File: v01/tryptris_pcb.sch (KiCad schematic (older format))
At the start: 131 parts, among them J1 USB_C_Receptacle_USB2.0, J2 I2C-L, J3 I2C-R, SW1 Reset, U1 ATmega32U4-AU, U2 MCP23017_SO, Y1 16Mhz

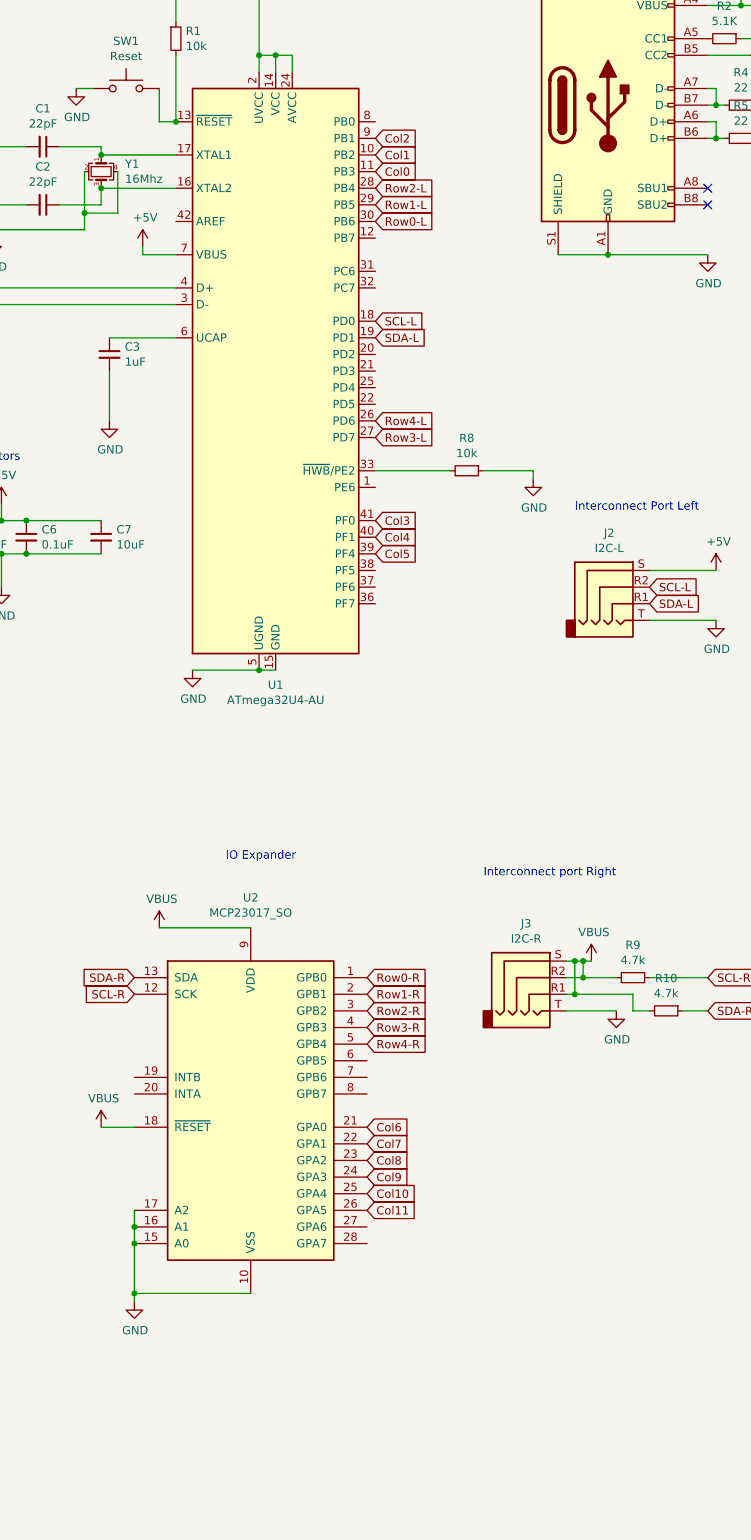
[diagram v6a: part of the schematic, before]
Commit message: Fix ERC and DRC errors.
Move right half to use VSS instead of GND and add power flags to remove
net links between sides.
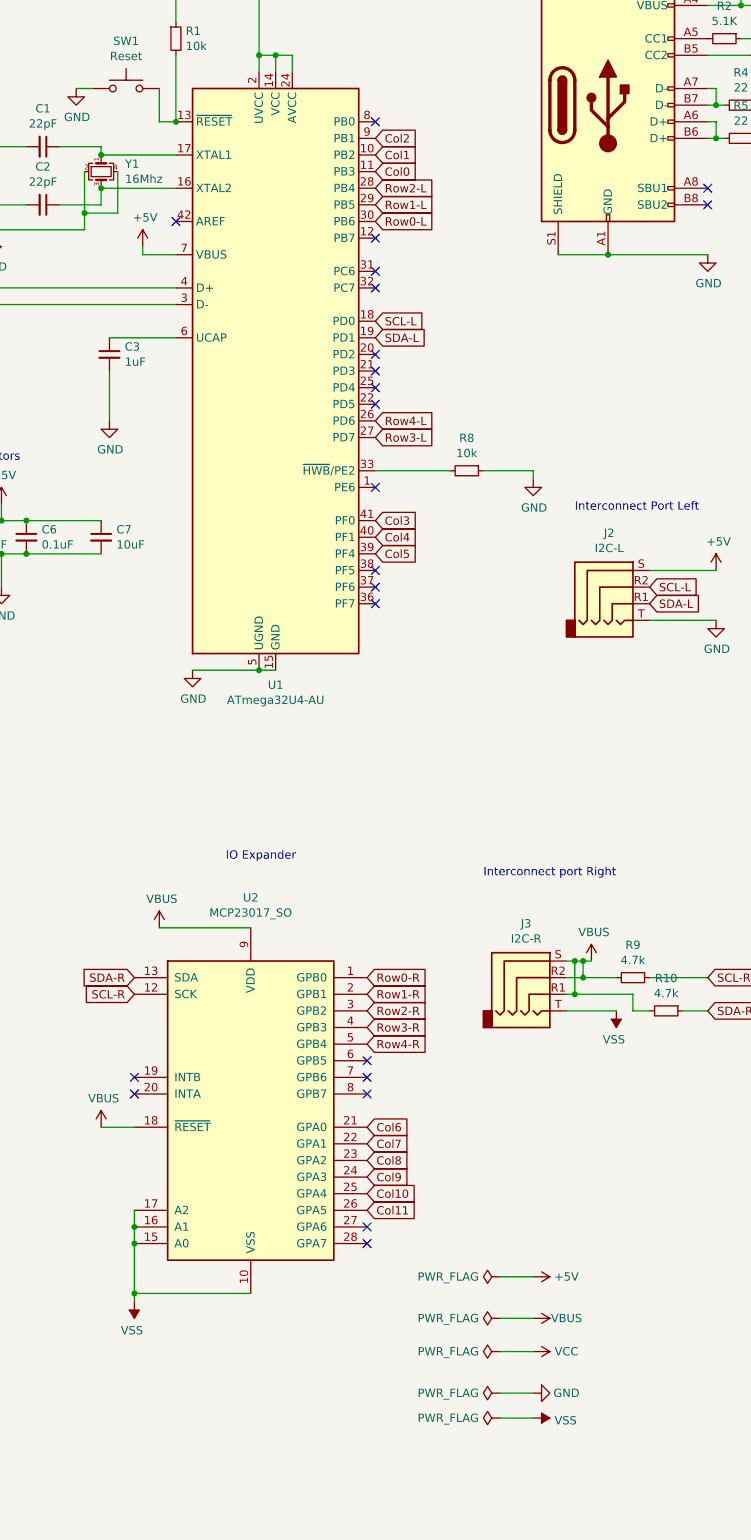
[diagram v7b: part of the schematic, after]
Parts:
- SW1: footprint random-keyboard-parts:PushButton_6x6mm_TH -> random-keyboard-parts:SKQG-1155865
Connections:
- net GND: no longer J3.T, U2.10 (VSS), U2.15 (A0), U2.16 (A1), U2.17 (A2)
- new net VSS: J3.T, U2.10 (VSS), U2.15 (A0), U2.16 (A1), U2.17 (A2)
- no-connect marks 2 -> 22
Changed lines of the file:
@@
 F 0 "SW1" H 2200 1835 50  0000 C CNN
 F 1 "Reset" H 2200 1744 50  0000 C CNN
-F 2 "random-keyboard-parts:PushButton_6x6mm_TH" H 2200 1750 50  0001 C CNN
+F 2 "random-keyboard-parts:SKQG-1155865" H 2200 1750 50  0001 C CNN
 F 3 "~" H 2200 1750 50  0001 C CNN
 	1    2200 1550
@@
 Text GLabel 3650 8300 2    50   Input ~ 0
 Col11
-$Comp
-L power:GND #PWR0114
-U 1 1 613EDEC9
-P 2250 8850
-F 0 "#PWR0114" H 2250 8600 50  0001 C CNN
-F 1 "GND" H 2255 8677 50  0000 C CNN
-F 2 "" H 2250 8850 50  0001 C CNN
-F 3 "" H 2250 8850 50  0001 C CNN
-	1    2250 8850
-	1    0    0    -1
-$EndComp
 Wire Wire Line
 	2950 8800 2250 8800
@@
 Wire Wire Line
 	5750 4750 5350 4750
-$Comp
-L power:GND #PWR0118
-U 1 1 61752755
-P 5150 7100
-F 0 "#PWR0118" H 5150 6850 50  0001 C CNN
-F 1 "GND" H 5155 6927 50  0000 C CNN
-F 2 "" H 5150 7100 50  0001 C CNN
-F 3 "" H 5150 7100 50  0001 C CNN
-	1    5150 7100
-	1    0    0    -1
-$EndComp
 Wire Wire Line
 	5150 7100 4850 7100
@@
 Wire Wire Line
 	1050 2750 2500 2750
+$Comp
+L power:PWR_FLAG #FLG0101
+U 1 1 617813AB
+P 4450 9400
+F 0 "#FLG0101" H 4450 9475 50  0001 C CNN
+F 1 "PWR_FLAG" V 4450 9527 50  0000 L CNN
+F 2 "" H 4450 9400 50  0001 C CNN
+F 3 "~" H 4450 9400 50  0001 C CNN
+	1    4450 9400
+	0    -1   -1   0
+$EndComp
+$Comp
+L power:GND #PWR0111
+U 1 1 61781F62
+P 4650 9400
+F 0 "#PWR0111" H 4650 9150 50  0001 C CNN
+F 1 "GND" V 4650 9200 50  0000 C CNN
+F 2 "" H 4650 9400 50  0001 C CNN
+F 3 "" H 4650 9400 50  0001 C CNN
+	1    4650 9400
+	0    -1   -1   0
+$EndComp
+Wire Wire Line
+	4450 9400 4650 9400
+$Comp
+L power:PWR_FLAG #FLG0102
+U 1 1 6179D4FD
+P 4450 8950
+F 0 "#FLG0102" H 4450 9025 50  0001 C CNN
+F 1 "PWR_FLAG" V 4450 9077 50  0000 L CNN
+F 2 "" H 4450 8950 50  0001 C CNN
+F 3 "~" H 4450 8950 50  0001 C CNN
+	1    4450 8950
+	0    -1   -1   0
+$EndComp
+Wire Wire Line
+	4450 8950 4650 8950
+NoConn ~ 2500 2350
+NoConn ~ 3700 2450
+NoConn ~ 3700 2650
+NoConn ~ 3700 2750
+NoConn ~ 3700 3150
+NoConn ~ 3700 3250
+NoConn ~ 3700 3350
+NoConn ~ 3700 3450
+NoConn ~ 3700 3950
+NoConn ~ 3700 4450
+NoConn ~ 3700 4550
+NoConn ~ 3700 4650
+NoConn ~ 3650 7400
+NoConn ~ 3650 7500
+NoConn ~ 3650 7600
+NoConn ~ 3650 8400
+NoConn ~ 3650 8500
+NoConn ~ 2250 7500
+NoConn ~ 2250 7600
+$Comp
+L power:PWR_FLAG #FLG0103
+U 1 1 61975930
+P 4450 8700
+F 0 "#FLG0103" H 4450 8775 50  0001 C CNN
+F 1 "PWR_FLAG" V 4450 8827 50  0000 L CNN
+F 2 "" H 4450 8700 50  0001 C CNN
+F 3 "~" H 4450 8700 50  0001 C CNN
+	1    4450 8700
+	0    -1   -1   0
+$EndComp
+$Comp
+L power:+5V #PWR0113
+U 1 1 6197725E
+P 4650 8700
+F 0 "#PWR0113" H 4650 8550 50  0001 C CNN
+F 1 "+5V" V 4650 8900 50  0000 C CNN
+F 2 "" H 4650 8700 50  0001 C CNN
+F 3 "" H 4650 8700 50  0001 C CNN
+	1    4650 8700
+	0    1    1    0
+$EndComp
+Wire Wire Line
+	4650 8700 4450 8700
+NoConn ~ 3700 1750
+$Comp
+L power:PWR_FLAG #FLG0104
+U 1 1 619BC24A
+P 4450 9150
+F 0 "#FLG0104" H 4450 9225 50  0001 C CNN
+F 1 "PWR_FLAG" V 4450 9277 50  0000 L CNN
+F 2 "" H 4450 9150 50  0001 C CNN
+F 3 "~" H 4450 9150 50  0001 C CNN
+	1    4450 9150
+	0    -1   -1   0
+$EndComp
+$Comp
+L power:VCC #PWR0115
+U 1 1 619BCAA9
+P 4650 9150
+F 0 "#PWR0115" H 4650 9000 50  0001 C CNN
+F 1 "VCC" V 4650 9350 50  0000 C CNN
+F 2 "" H 4650 9150 50  0001 C CNN
+F 3 "" H 4650 9150 50  0001 C CNN
+	1    4650 9150
+	0    1    1    0
+$EndComp
+Wire Wire Line
+	4650 9150 4450 9150
+$Comp
+L power:VSS #PWR?
+U 1 1 61A602BB
+P 5150 7100
+F 0 "#PWR?" H 5150 6950 50  0001 C CNN
+F 1 "VSS" H 5165 7273 50  0000 C CNN
+F 2 "" H 5150 7100 50  0001 C CNN
+F 3 "" H 5150 7100 50  0001 C CNN
+	1    5150 7100
+	-1   0    0    1
+$EndComp
+$Comp
+L power:VBUS #PWR0112
+U 1 1 617B19F5
+P 4650 8950
+F 0 "#PWR0112" H 4650 8800 50  0001 C CNN
+F 1 "VBUS" V 4650 9150 50  0000 C CNN
+F 2 "" H 4650 8950 50  0001 C CNN
+F 3 "" H 4650 8950 50  0001 C CNN
+	1    4650 8950
+	0    1    1    0
+$EndComp
+$Comp
+L power:PWR_FLAG #FLG?
+U 1 1 61AF2E3C
+P 4450 9550
+F 0 "#FLG?" H 4450 9625 50  0001 C CNN
+F 1 "PWR_FLAG" V 4450 9677 50  0000 L CNN
+F 2 "" H 4450 9550 50  0001 C CNN
+F 3 "~" H 4450 9550 50  0001 C CNN
+	1    4450 9550
+	0    -1   -1   0
+$EndComp
+$Comp
+L power:VSS #PWR?
+U 1 1 61AF36DB
+P 4650 9550
+F 0 "#PWR?" H 4650 9400 50  0001 C CNN
+F 1 "VSS" V 4665 9678 50  0000 L CNN
+F 2 "" H 4650 9550 50  0001 C CNN
+F 3 "" H 4650 9550 50  0001 C CNN
+	1    4650 9550
+	0    1    1    0
+$EndComp
+Wire Wire Line
+	4450 9550 4650 9550
+$Comp
+L power:VSS #PWR?
+U 1 1 61B1EC51
+P 2250 8850
+F 0 "#PWR?" H 2250 8700 50  0001 C CNN
+F 1 "VSS" H 2265 9023 50  0000 C CNN
+F 2 "" H 2250 8850 50  0001 C CNN
+F 3 "" H 2250 8850 50  0001 C CNN
+	1    2250 8850
+	-1   0    0    1
+$EndComp
 $EndSCHEMATC

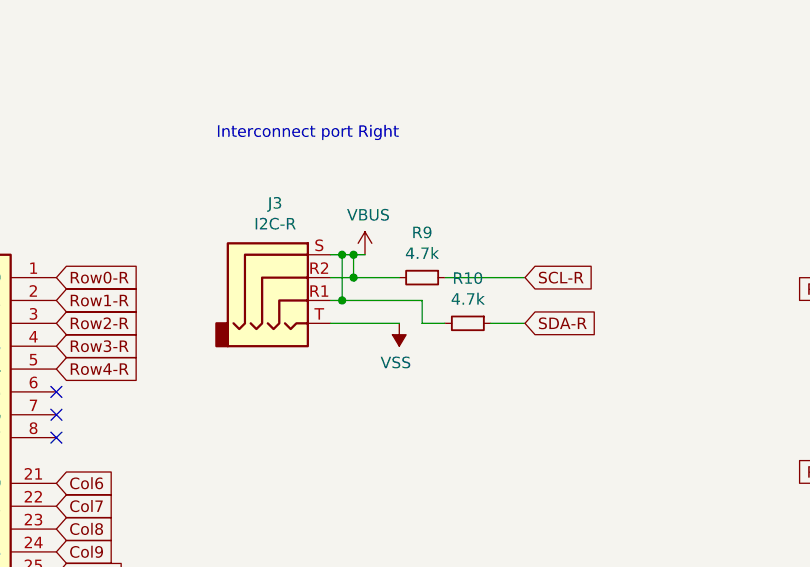
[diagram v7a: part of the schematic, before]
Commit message: Fix TRRS wiring and improve grounding
* Don't route gnd for trrs through the crystal. Instead send it around the
  crystal and into the larger ground plane of the MCU.
* Fix the right side wiring. 5V should pass through the resisitors
  before being connected to the signal wires. The goal is to provide
  background voltage not flood the signal.
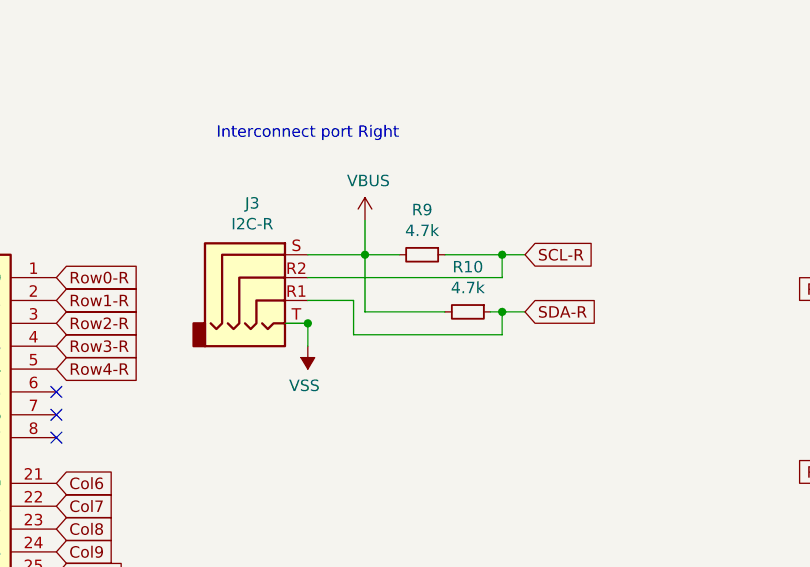
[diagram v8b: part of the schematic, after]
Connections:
- net SCL-R: now also J3.R2
- net SDA-R: now also J3.R1
- net VBUS: no longer J3.R1, J3.R2
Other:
- moved on the sheet: J3, R10, R9
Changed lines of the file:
@@
 Text GLabel 3700 2950 2    50   Input ~ 0
 SCL-L
-Text GLabel 5700 7100 2    50   Input ~ 0
+Text GLabel 5700 7050 2    50   Input ~ 0
 SDA-R
-Text GLabel 5700 6900 2    50   Input ~ 0
+Text GLabel 5700 6800 2    50   Input ~ 0
 SCL-R
 Text Notes 4350 6300 0    50   ~ 0
@@
 Wire Wire Line
 	5750 4750 5350 4750
-Wire Wire Line
-	5150 7100 4850 7100
 $Comp
 L power:VBUS #PWR0119
 U 1 1 61761FE9
-P 5000 6800
-F 0 "#PWR0119" H 5000 6650 50  0001 C CNN
-F 1 "VBUS" H 5015 6973 50  0000 C CNN
-F 2 "" H 5000 6800 50  0001 C CNN
-F 3 "" H 5000 6800 50  0001 C CNN
-	1    5000 6800
+P 5000 6650
+F 0 "#PWR0119" H 5000 6500 50  0001 C CNN
+F 1 "VBUS" H 5015 6823 50  0000 C CNN
+F 2 "" H 5000 6650 50  0001 C CNN
+F 3 "" H 5000 6650 50  0001 C CNN
+	1    5000 6650
 	1    0    0    -1
 $EndComp
@@
 L Device:R_Small R9
 U 1 1 6181A4E0
-P 5250 6900
-F 0 "R9" V 5054 6900 50  0000 C CNN
-F 1 "4.7k" V 5145 6900 50  0000 C CNN
-F 2 "Resistor_SMD:R_0805_2012Metric" H 5250 6900 50  0001 C CNN
-F 3 "~" H 5250 6900 50  0001 C CNN
-	1    5250 6900
-	0    1    1    0
-$EndComp
-Wire Wire Line
-	5000 6800 4950 6800
-Wire Wire Line
-	4850 6900 4950 6900
-Wire Wire Line
-	4950 6800 4950 6900
-Connection ~ 4950 6800
-Wire Wire Line
-	4950 6800 4900 6800
-Connection ~ 4950 6900
-Wire Wire Line
-	4950 6900 5150 6900
+P 5250 6800
+F 0 "R9" V 5054 6800 50  0000 C CNN
+F 1 "4.7k" V 5145 6800 50  0000 C CNN
+F 2 "Resistor_SMD:R_0805_2012Metric" H 5250 6800 50  0001 C CNN
+F 3 "~" H 5250 6800 50  0001 C CNN
+	1    5250 6800
+	0    1    1    0
+$EndComp
 $Comp
 L Device:R_Small R10
 U 1 1 618545B8
-P 5450 7100
-F 0 "R10" V 5254 7100 50  0000 C CNN
-F 1 "4.7k" V 5345 7100 50  0000 C CNN
-F 2 "Resistor_SMD:R_0805_2012Metric" H 5450 7100 50  0001 C CNN
-F 3 "~" H 5450 7100 50  0001 C CNN
-	1    5450 7100
-	0    1    1    0
-$EndComp
-Wire Wire Line
-	5350 7100 5250 7100
-Wire Wire Line
-	5250 7100 5250 7000
-Wire Wire Line
-	5250 7000 4900 7000
-Wire Wire Line
-	4900 6800 4900 7000
-Connection ~ 4900 6800
-Wire Wire Line
-	4900 6800 4850 6800
-Connection ~ 4900 7000
-Wire Wire Line
-	4900 7000 4850 7000
+P 5450 7050
+F 0 "R10" V 5254 7050 50  0000 C CNN
+F 1 "4.7k" V 5345 7050 50  0000 C CNN
+F 2 "Resistor_SMD:R_0805_2012Metric" H 5450 7050 50  0001 C CNN
+F 3 "~" H 5450 7050 50  0001 C CNN
+	1    5450 7050
+	0    1    1    0
+$EndComp
 $Comp
 L power:+5V #PWR0122
@@
 Wire Wire Line
 	5750 4450 5350 4450
-Wire Wire Line
-	5700 7100 5550 7100
-Wire Wire Line
-	5350 6900 5700 6900
 $Comp
 L Connector:USB_C_Receptacle_USB2.0 J1
@@
 L Connector:AudioJack4 J3
 U 1 1 6217961C
-P 4650 6900
-F 0 "J3" H 4607 7225 50  0000 C CNN
-F 1 "I2C-R" H 4607 7134 50  0000 C CNN
-F 2 "Connector_Audio:Jack_3.5mm_PJ320E_Horizontal" H 4650 6900 50  0001 C CNN
-F 3 "~" H 4650 6900 50  0001 C CNN
-	1    4650 6900
+P 4550 6900
+F 0 "J3" H 4507 7225 50  0000 C CNN
+F 1 "I2C-R" H 4507 7134 50  0000 C CNN
+F 2 "Connector_Audio:Jack_3.5mm_PJ320E_Horizontal" H 4550 6900 50  0001 C CNN
+F 3 "~" H 4550 6900 50  0001 C CNN
+	1    4550 6900
 	1    0    0    -1
 $EndComp
@@
 L power:VSS #PWR?
 U 1 1 61A602BB
-P 5150 7100
-F 0 "#PWR?" H 5150 6950 50  0001 C CNN
-F 1 "VSS" H 5165 7273 50  0000 C CNN
-F 2 "" H 5150 7100 50  0001 C CNN
-F 3 "" H 5150 7100 50  0001 C CNN
-	1    5150 7100
+P 4750 7200
+F 0 "#PWR?" H 4750 7050 50  0001 C CNN
+F 1 "VSS" H 4765 7373 50  0000 C CNN
+F 2 "" H 4750 7200 50  0001 C CNN
+F 3 "" H 4750 7200 50  0001 C CNN
+	1    4750 7200
 	-1   0    0    1
 $EndComp
@@
 	-1   0    0    1
 $EndComp
+Wire Wire Line
+	4650 7100 4750 7100
+Wire Wire Line
+	5550 7050 5600 7050
+Wire Wire Line
+	5000 6800 5000 6650
+Wire Wire Line
+	4750 6800 5000 6800
+Connection ~ 5000 6800
+Wire Wire Line
+	5000 6800 5150 6800
+Wire Wire Line
+	5000 7050 5350 7050
+Wire Wire Line
+	5600 6900 5600 6800
+Wire Wire Line
+	5350 6800 5600 6800
+Connection ~ 5600 6800
+Wire Wire Line
+	5600 6800 5700 6800
+Wire Wire Line
+	5000 6800 5000 7050
+Wire Wire Line
+	4750 6900 5600 6900
+Wire Wire Line
+	4750 7100 4750 7200
+Connection ~ 4750 7100
+Wire Wire Line
+	4750 7000 4950 7000
+Wire Wire Line
+	4950 7000 4950 7150
+Wire Wire Line
+	4950 7150 5600 7150
+Wire Wire Line
+	5600 7150 5600 7050
+Connection ~ 5600 7050
+Wire Wire Line
+	5600 7050 5700 7050
 $EndSCHEMATC
